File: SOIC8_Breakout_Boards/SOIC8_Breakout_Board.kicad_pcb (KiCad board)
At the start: 2 copper layers, 25 x 25 mm, 6 parts, among them J1 Conn_01x04, J2 Conn_01x04, J3 Conn_01x01, J4 Conn_01x01

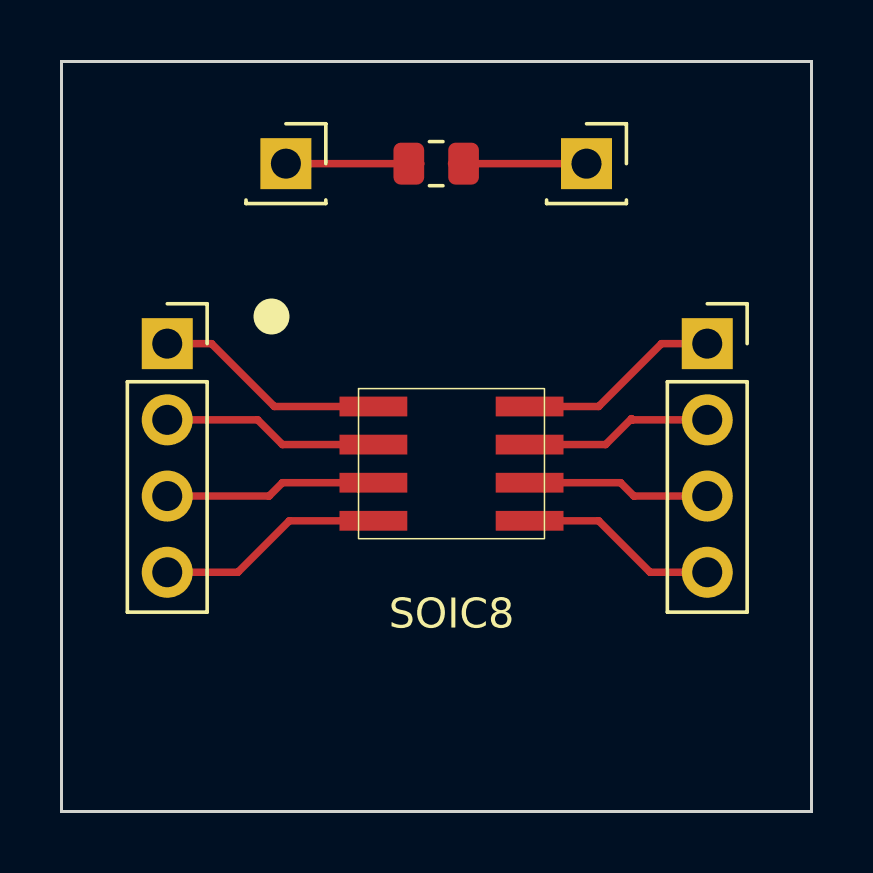
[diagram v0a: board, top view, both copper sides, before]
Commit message: Fixed warnings on all SOIC boards
Ensured that silkscreen traces didn't intersect solder masks and name/board information is visible on the front of the board rather than the back
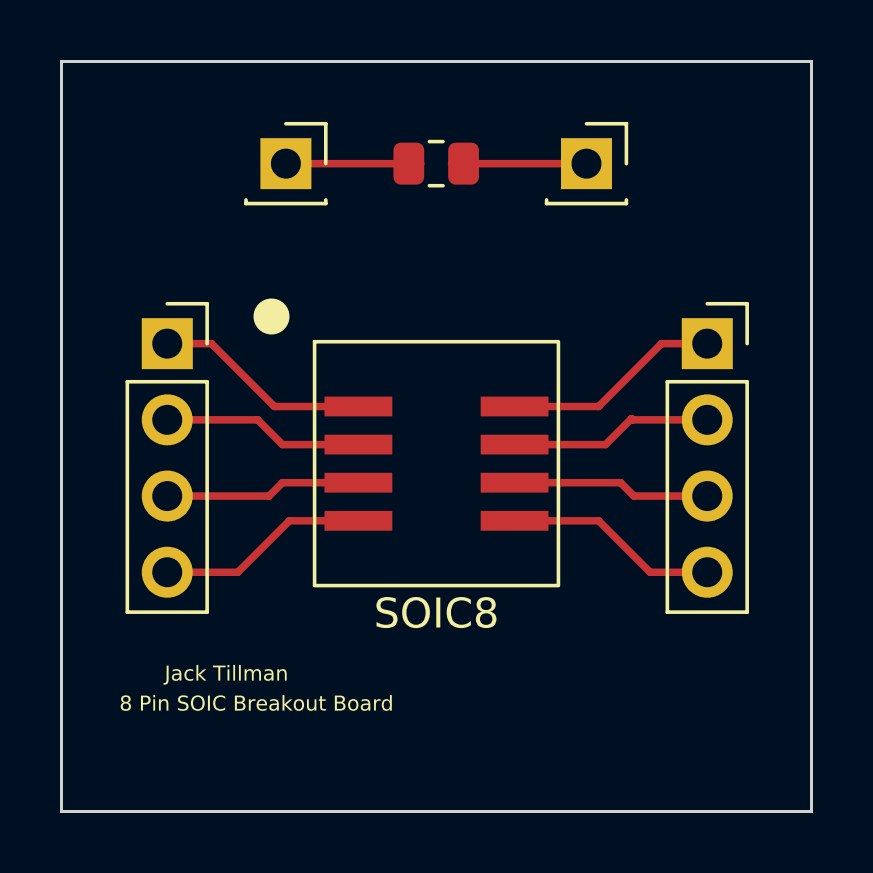
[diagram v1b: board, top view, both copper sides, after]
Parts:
- moved SOIC8 0.50 mm to (154.5, 101.4)
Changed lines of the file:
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@@
   )
   (footprint "SOIC_Footprints:8_Pin_SOIC_Board" (layer "F.Cu")
-    (at 155 101.405)
+    (at 154.5 101.405)
     (property "Sheetfile" "8Pin_Testing_Board.kicad_sch")
     (property "Sheetname" "")
@@
       (effects (font (size 1 1) (thickness 0.15)))
     )
-    (fp_rect (start -3.0988 -2.5019) (end 3.0988 2.5019) (layer "F.SilkS") (width 0.05) (fill none))
-    (fp_rect (start -4.064 -4.064) (end 4.064 4.064) (layer "F.Fab") (width 0.12) (fill none))
+    (fp_rect (start -4.064 -4.064) (end 4.064 4.064) (layer "F.SilkS") (width 0.12) (fill none))
+    (fp_rect (start -3.0988 -2.5019) (end 3.0988 2.5019) (layer "F.Fab") (width 0.05) (fill none))
     (pad "1" smd rect (at -2.6035 -1.905) (size 2.2606 0.6604) (layers "F.Cu" "F.Paste" "F.Mask")
       (net 1 "Net-(J1-Pad1)") (pintype "unspecified"))
@@
   (gr_circle (center 149 96.5) (end 149.5 96.5) (layer "F.SilkS") (width 0.2) (fill solid))
   (gr_rect (start 142 88) (end 167 113) (layer "Edge.Cuts") (width 0.1) (fill none))
-  (gr_text "8 Pin SOIC Breakout Board" (at 148.5 109.405) (layer "B.SilkS")
+  (gr_text "8 Pin SOIC Breakout Board" (at 148.5 109.405) (layer "F.SilkS")
     (effects (font (size 0.5 0.5) (thickness 0.05)))
   )
-  (gr_text "Jack Tillman" (at 147.5 108.405) (layer "B.SilkS")
+  (gr_text "Jack Tillman" (at 147.5 108.405) (layer "F.SilkS")
     (effects (font (size 0.5 0.5) (thickness 0.05)))
   )

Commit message: Finished tracing the SOIC20 board
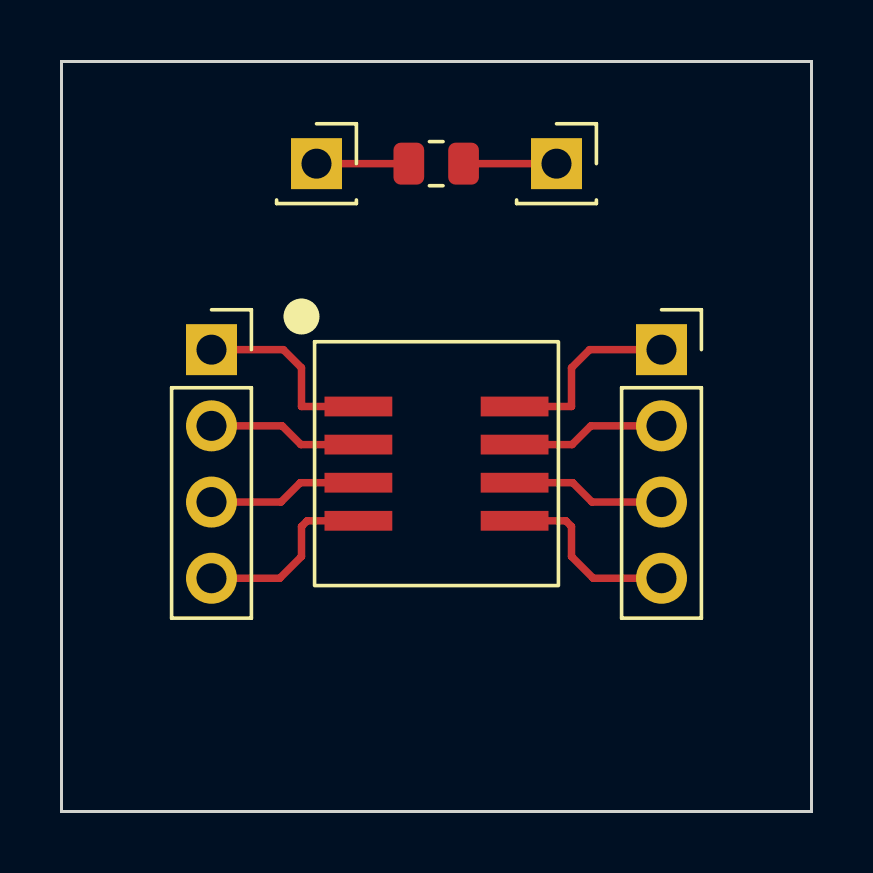
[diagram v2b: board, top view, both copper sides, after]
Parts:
- moved J2 1.54 mm to (162.0, 97.6)
- moved J1 1.49 mm to (147.0, 97.6)
- moved J4 1.02 mm to (150.5, 91.4)
- moved J3 1.00 mm to (158.5, 91.4)
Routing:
- net Net-(J2-Pad2): track 6.80 -> 5.16 mm
- net Net-(J1-Pad2): track 6.71 -> 5.16 mm
- net Net-(J2-Pad3): track 6.61 -> 5.16 mm
- net Net-(J4-Pad1): track 4.50 -> 3.08 mm
- net Net-(J1-Pad3): track 6.56 -> 5.16 mm
- net Net-(J3-Pad1): track 3.98 -> 3.10 mm
- net Net-(J2-Pad4): track 7.13 -> 6.28 mm
- net Net-(J2-Pad1): track 7.29 -> 6.44 mm
- net Net-(J1-Pad4): track 7.08 -> 6.28 mm
- net Net-(J1-Pad1): track 7.24 -> 6.44 mm
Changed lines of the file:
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@@
   (net 10 "Net-(J2-Pad4)")
   (footprint "Connector_PinSocket_2.54mm:PinSocket_1x04_P2.54mm_Vertical" (layer "F.Cu")
-    (at 145.525 97.405)
+    (at 147 97.605)
     (descr "Through hole straight socket strip, 1x04, 2.54mm pitch, single row (from Kicad 4.0.7), script generated")
     (tags "Through hole socket strip THT 1x04 2.54mm single row")
@@
   )
   (footprint "Connector_PinSocket_2.54mm:PinSocket_1x04_P2.54mm_Vertical" (layer "F.Cu")
-    (at 163.525 97.405)
+    (at 162 97.605)
     (descr "Through hole straight socket strip, 1x04, 2.54mm pitch, single row (from Kicad 4.0.7), script generated")
     (tags "Through hole socket strip THT 1x04 2.54mm single row")
@@
     (property "Sheetname" "")
     (attr through_hole)
-    (fp_text reference "SOIC8" (at 0 5 unlocked) (layer "F.SilkS")
-      (effects (font (size 1 1) (thickness 0.15)))
+    (fp_text reference "SOIC8" (at 0 0.095 unlocked) (layer "B.SilkS")
+      (effects (font (size 2.5 2.5) (thickness 0.15)) (justify mirror))
     )
     (fp_text value "8_Pin_SOIC_Board" (at 0 5.588 unlocked) (layer "F.Fab") hide
@@
   )
   (footprint "Connector_PinSocket_2.54mm:PinSocket_1x01_P2.54mm_Vertical" (layer "F.Cu")
-    (at 159.5 91.405)
+    (at 158.5 91.405)
     (descr "Through hole straight socket strip, 1x01, 2.54mm pitch, single row (from Kicad 4.0.7), script generated")
     (tags "Through hole socket strip THT 1x01 2.54mm single row")
@@
   )
   (footprint "Connector_PinSocket_2.54mm:PinSocket_1x01_P2.54mm_Vertical" (layer "F.Cu")
-    (at 149.48 91.405)
+    (at 150.5 91.405)
     (descr "Through hole straight socket strip, 1x01, 2.54mm pitch, single row (from Kicad 4.0.7), script generated")
     (tags "Through hole socket strip THT 1x01 2.54mm single row")
@@
     )
   )
-  (gr_circle (center 149 96.5) (end 149.5 96.5) (layer "F.SilkS") (width 0.2) (fill solid))
+  (gr_circle (center 150 96.5) (end 150.5 96.5) (layer "F.SilkS") (width 0.2) (fill solid))
   (gr_rect (start 142 88) (end 167 113) (layer "Edge.Cuts") (width 0.1) (fill none))
-  (gr_text "8 Pin SOIC Breakout Board" (at 148.5 109.405) (layer "F.SilkS")
-    (effects (font (size 0.5 0.5) (thickness 0.05)))
-  )
-  (gr_text "Jack Tillman" (at 147.5 108.405) (layer "F.SilkS")
-    (effects (font (size 0.5 0.5) (thickness 0.05)))
-  )
-  (segment (start 149.095 99.5) (end 147 97.405) (width 0.25) (layer "F.Cu") (net 1))
-  (segment (start 147 97.405) (end 145.525 97.405) (width 0.25) (layer "F.Cu") (net 1))
-  (segment (start 151.8965 99.5) (end 149.095 99.5) (width 0.25) (layer "F.Cu") (net 1))
-  (segment (start 149.365 100.77) (end 148.54 99.945) (width 0.25) (layer "F.Cu") (net 2))
-  (segment (start 148.54 99.945) (end 145.525 99.945) (width 0.25) (layer "F.Cu") (net 2))
-  (segment (start 151.8965 100.77) (end 149.365 100.77) (width 0.25) (layer "F.Cu") (net 2))
-  (segment (start 149.365 102.04) (end 148.92 102.485) (width 0.25) (layer "F.Cu") (net 3))
-  (segment (start 148.92 102.485) (end 145.525 102.485) (width 0.25) (layer "F.Cu") (net 3))
-  (segment (start 151.8965 102.04) (end 149.365 102.04) (width 0.25) (layer "F.Cu") (net 3))
-  (segment (start 149.595 103.31) (end 147.88 105.025) (width 0.25) (layer "F.Cu") (net 4))
-  (segment (start 147.88 105.025) (end 145.525 105.025) (width 0.25) (layer "F.Cu") (net 4))
-  (segment (start 151.8965 103.31) (end 149.595 103.31) (width 0.25) (layer "F.Cu") (net 4))
-  (segment (start 159.905 99.5) (end 162 97.405) (width 0.25) (layer "F.Cu") (net 5))
-  (segment (start 162 97.405) (end 163.525 97.405) (width 0.25) (layer "F.Cu") (net 5))
-  (segment (start 157.1035 99.5) (end 159.905 99.5) (width 0.25) (layer "F.Cu") (net 5))
-  (segment (start 161.04 99.945) (end 163.525 99.945) (width 0.25) (layer "F.Cu") (net 6))
-  (segment (start 161 99.905) (end 161.04 99.945) (width 0.25) (layer "F.Cu") (net 6))
-  (segment (start 160.135 100.77) (end 161 99.905) (width 0.25) (layer "F.Cu") (net 6))
-  (segment (start 157.1035 100.77) (end 160.135 100.77) (width 0.25) (layer "F.Cu") (net 6))
-  (segment (start 160.635 102.04) (end 161.08 102.485) (width 0.25) (layer "F.Cu") (net 7))
-  (segment (start 157.1035 102.04) (end 160.635 102.04) (width 0.25) (layer "F.Cu") (net 7))
-  (segment (start 161.08 102.485) (end 163.525 102.485) (width 0.25) (layer "F.Cu") (net 7))
-  (segment (start 158.98 91.405) (end 155 91.405) (width 0.25) (layer "F.Cu") (net 8))
-  (segment (start 153.98 91.405) (end 149.48 91.405) (width 0.25) (layer "F.Cu") (net 9))
-  (segment (start 159.905 103.31) (end 161.62 105.025) (width 0.25) (layer "F.Cu") (net 10))
-  (segment (start 157.1035 103.31) (end 159.905 103.31) (width 0.25) (layer "F.Cu") (net 10))
-  (segment (start 161.62 105.025) (end 163.525 105.025) (width 0.25) (layer "F.Cu") (net 10))
+  (gr_text "8 Pin SOIC Breakout Board" (at 161.5 112) (layer "B.SilkS")
+    (effects (font (size 0.5 0.5) (thickness 0.05)) (justify mirror))
+  )
+  (gr_text "Jack Tillman" (at 160.5 111) (layer "B.SilkS")
+    (effects (font (size 0.5 0.5) (thickness 0.05)) (justify mirror))
+  )
+  (segment (start 149.395 97.605) (end 150 98.21) (width 0.25) (layer "F.Cu") (net 1))
+  (segment (start 150 99.5) (end 151.8965 99.5) (width 0.25) (layer "F.Cu") (net 1))
+  (segment (start 147 97.605) (end 149.395 97.605) (width 0.25) (layer "F.Cu") (net 1))
+  (segment (start 150 98.21) (end 150 99.5) (width 0.25) (layer "F.Cu") (net 1))
+  (segment (start 147 100.145) (end 149.355 100.145) (width 0.25) (layer "F.Cu") (net 2))
+  (segment (start 149.98 100.77) (end 151.8965 100.77) (width 0.25) (layer "F.Cu") (net 2))
+  (segment (start 149.355 100.145) (end 149.98 100.77) (width 0.25) (layer "F.Cu") (net 2))
+  (segment (start 149.96 102.04) (end 151.8965 102.04) (width 0.25) (layer "F.Cu") (net 3))
+  (segment (start 147 102.685) (end 149.315 102.685) (width 0.25) (layer "F.Cu") (net 3))
+  (segment (start 149.315 102.685) (end 149.96 102.04) (width 0.25) (layer "F.Cu") (net 3))
+  (segment (start 149.275 105.225) (end 150 104.5) (width 0.25) (layer "F.Cu") (net 4))
+  (segment (start 150.19 103.31) (end 151.8965 103.31) (width 0.25) (layer "F.Cu") (net 4))
+  (segment (start 150 104.5) (end 150 103.5) (width 0.25) (layer "F.Cu") (net 4))
+  (segment (start 150 103.5) (end 150.19 103.31) (width 0.25) (layer "F.Cu") (net 4))
+  (segment (start 147 105.225) (end 149.275 105.225) (width 0.25) (layer "F.Cu") (net 4))
+  (segment (start 162 97.605) (end 159.605 97.605) (width 0.25) (layer "F.Cu") (net 5))
+  (segment (start 159.605 97.605) (end 159 98.21) (width 0.25) (layer "F.Cu") (net 5))
+  (segment (start 159 99.5) (end 157.1035 99.5) (width 0.25) (layer "F.Cu") (net 5))
+  (segment (start 159 98.21) (end 159 99.5) (width 0.25) (layer "F.Cu") (net 5))
+  (segment (start 159.645 100.145) (end 159.02 100.77) (width 0.25) (layer "F.Cu") (net 6))
+  (segment (start 162 100.145) (end 159.645 100.145) (width 0.25) (layer "F.Cu") (net 6))
+  (segment (start 159.02 100.77) (end 157.1035 100.77) (width 0.25) (layer "F.Cu") (net 6))
+  (segment (start 162 102.685) (end 159.685 102.685) (width 0.25) (layer "F.Cu") (net 7))
+  (segment (start 159.04 102.04) (end 157.1035 102.04) (width 0.25) (layer "F.Cu") (net 7))
+  (segment (start 159.685 102.685) (end 159.04 102.04) (width 0.25) (layer "F.Cu") (net 7))
+  (segment (start 158.5 91.405) (end 155.4025 91.405) (width 0.25) (layer "F.Cu") (net 8))
+  (segment (start 150.5 91.405) (end 153.5775 91.405) (width 0.25) (layer "F.Cu") (net 9))
+  (segment (start 158.81 103.31) (end 157.1035 103.31) (width 0.25) (layer "F.Cu") (net 10))
+  (segment (start 159 103.5) (end 158.81 103.31) (width 0.25) (layer "F.Cu") (net 10))
+  (segment (start 159.725 105.225) (end 159 104.5) (width 0.25) (layer "F.Cu") (net 10))
+  (segment (start 162 105.225) (end 159.725 105.225) (width 0.25) (layer "F.Cu") (net 10))
+  (segment (start 159 104.5) (end 159 103.5) (width 0.25) (layer "F.Cu") (net 10))
 )
